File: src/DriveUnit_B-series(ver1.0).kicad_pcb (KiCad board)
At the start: 2 copper layers, 65.7 x 51 mm, 57 parts, among them IC1 A3921, SW1 TVAF06-A020B-R, SW2 TVAF06-A020B-R, SW3 THAF01-NC-R, SW4 SS-12D00G3

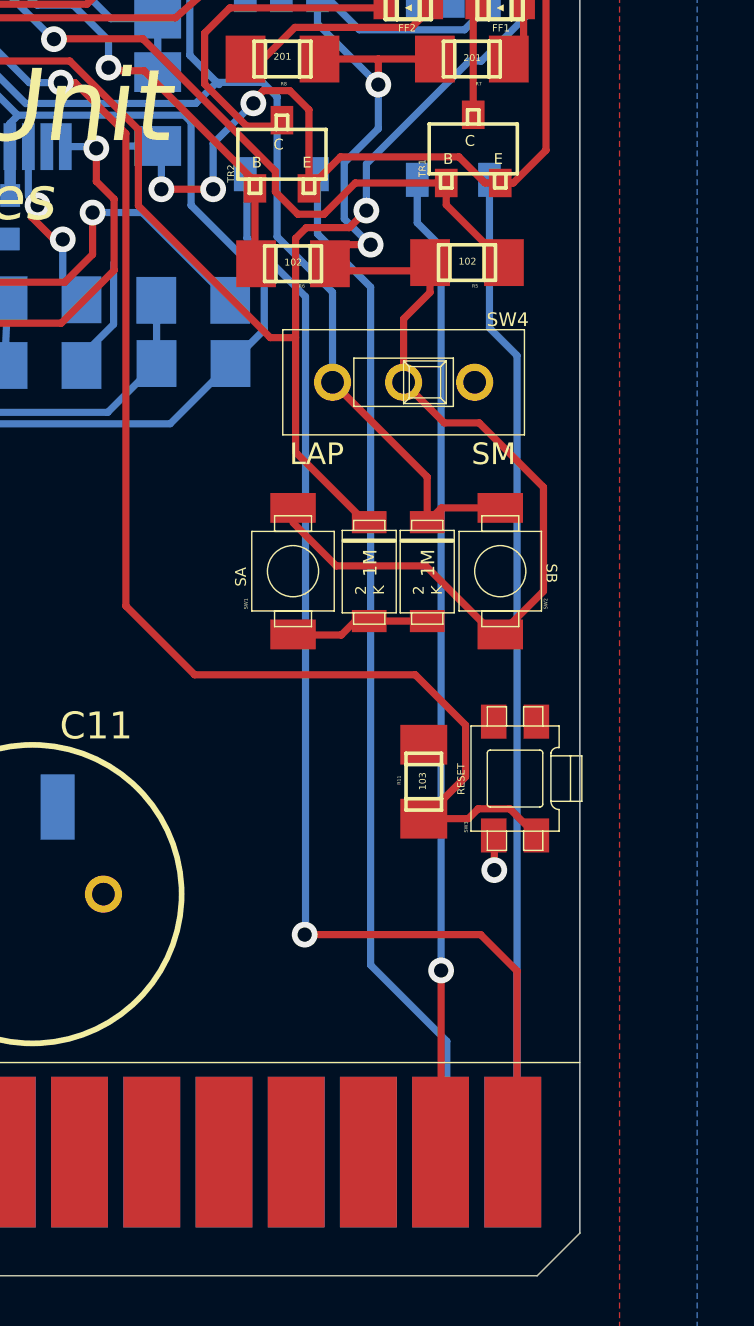
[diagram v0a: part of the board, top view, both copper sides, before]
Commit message: フォトカプラLED入力に200ohm抵抗付けた
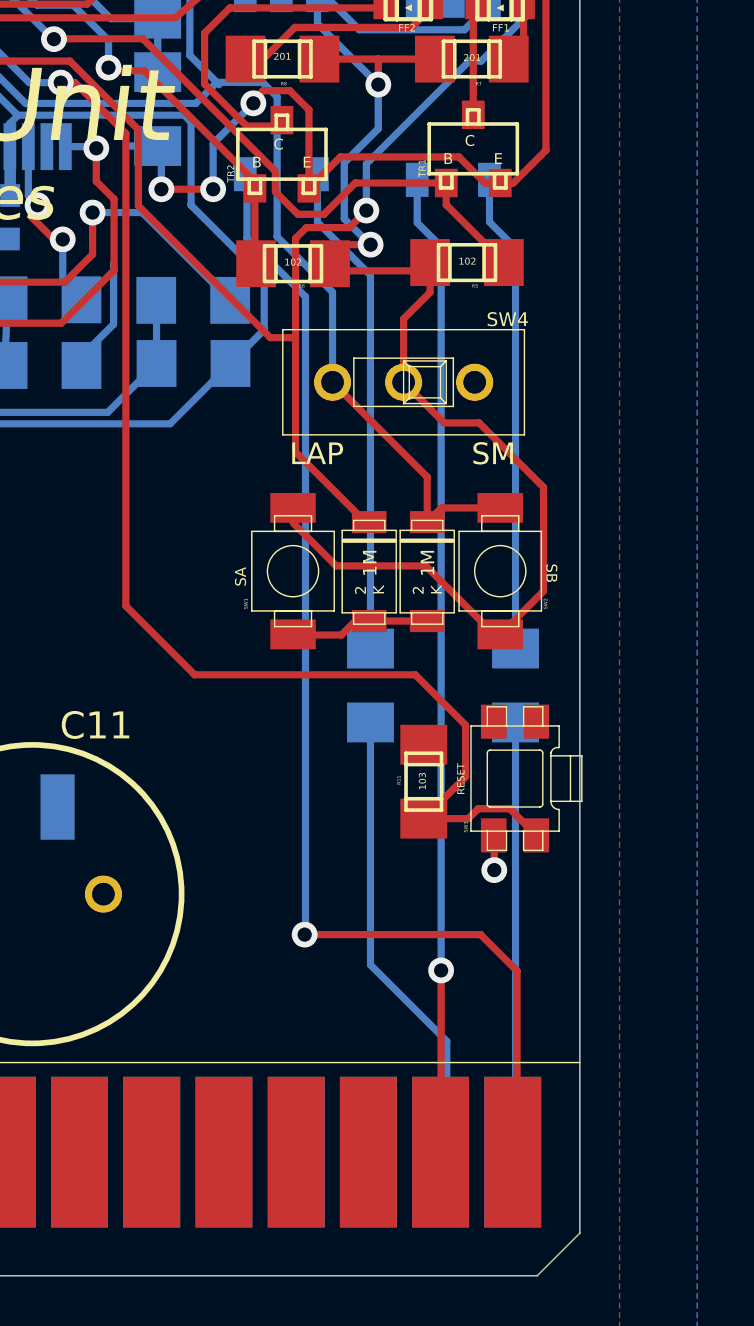
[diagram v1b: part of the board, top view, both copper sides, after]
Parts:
- added R17: RG2012N-201-W-T1, DriveUnit_B-series(ver1.0):RG2012, B.Cu at (174.0, 108.4)
- added R4: RG2012N-201-W-T1, DriveUnit_B-series(ver1.0):RG2012, B.Cu at (179.1, 108.4)
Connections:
- TLP1 pad 1: /DIR_IN -> Net-(R4-PadLEFT)
- TLP2 pad 1: /VCC_IN -> Net-(R17-PadLEFT)
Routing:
- net /VCC_IN: track 36.4 -> 16.3 mm
- net /DIR_IN: track 34.7 -> 15.4 mm
- net Net-(R17-PadLEFT): track 0.00 -> 17.5 mm
- net Net-(R4-PadLEFT): track 0.00 -> 16.9 mm

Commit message: シルクの修正
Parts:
- moved C10 1.36 mm to (153.5, 108.8), turned to 180 degrees
- moved C11 0.74 mm to (162.0, 116.3)
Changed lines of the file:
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@@
     (add_net VCC)
+  )
+  (module "彼女(仮)_回路図:35PZJ330M10X9" (layer Top)
+    (at 161.96 116.35 90)
+    (fp_text reference C11 (at 4.83876 5.74752 180) (layer F.SilkS)
+      (effects (font (size 0.95 0.95) (thickness 0.076)) (justify right bottom))
+    )
+    (fp_text value 35PZJ330M10X9 (at 0 0 90) (layer F.SilkS) hide
+      (effects (font (size 1.27 1.27) (thickness 0.15)))
+    )
+    (fp_circle (center 0 0) (end 5.25 0) (layer F.SilkS) (width 0.2))
+    (fp_line (start 5.2705 0) (end -5.25 0) (layer F.SilkS) (width 0.12))
+    (fp_poly (pts (xy 5.24 0.64) (xy 5.06 1.47) (xy 4.75 2.26) (xy 4.38 2.89)
+      (xy 3.85 3.56) (xy 3.01 4.28) (xy 2.15 4.77) (xy 0.89 5.18)
+      (xy -0.23 5.27) (xy -1.28 5.1) (xy -2.65 4.55) (xy -3.62 3.85)
+      (xy -4.63 2.58) (xy -5.03 1.62) (xy -5.22 0.58) (xy -5.25 0)
+      (xy 5.2705 0)) (layer F.SilkS) (width 0.1))
+    (pad C thru_hole circle (at 0 2.5 90) (size 1.308 1.308) (drill 0.8) (layers *.Cu *.Mask)
+      (net 2 GND) (solder_mask_margin 0.1016))
+    (pad A thru_hole circle (at 0 -2.5 90) (size 1.308 1.308) (drill 0.8) (layers *.Cu *.Mask)
+      (net 1 VCC) (solder_mask_margin 0.1016))
+  )
+  (module "彼女(仮)_回路図:35PZJ330M10X9" (layer Top)
+    (at 153.511218 108.784261 180)
+    (fp_text reference C10 (at 3.051218 4.514261 180) (layer F.SilkS)
+      (effects (font (size 0.95 0.95) (thickness 0.076)) (justify right bottom))
+    )
+    (fp_text value 35PZJ330M10X9 (at 0 0) (layer F.SilkS) hide
+      (effects (font (size 1.27 1.27) (thickness 0.15)))
+    )
+    (fp_circle (center 0 0) (end 5.25 0) (layer F.SilkS) (width 0.2))
+    (fp_line (start -5.25 0) (end 5.25 0) (layer F.SilkS) (width 0.12))
+    (fp_poly (pts (xy 5.26 0.16) (xy 5.11 1.23) (xy 4.77 2.28) (xy 4.06 3.4)
+      (xy 2.63 4.62) (xy 1.36 5.16) (xy -0.5 5.27) (xy -1.93 4.9)
+      (xy -3.31 4.14) (xy -4.08 3.35) (xy -4.64 2.55) (xy -4.98 1.76)
+      (xy -5.17 0.99) (xy -5.25 0) (xy 5.25 0)) (layer F.SilkS) (width 0.1))
+    (pad A thru_hole circle (at 0 -2.5 180) (size 1.308 1.308) (drill 0.8) (layers *.Cu *.Mask)
+      (net 1 VCC) (solder_mask_margin 0.1016))
+    (pad C thru_hole circle (at 0 2.5 180) (size 1.308 1.308) (drill 0.8) (layers *.Cu *.Mask)
+      (net 2 GND) (solder_mask_margin 0.1016))
   )
   (module "DriveUnit_B-series(ver1.0):RG2012" (layer Bottom)
@@
       (net 13 "Net-(C6-PadP$1)") (solder_mask_margin 0.1016))
   )
-  (module "彼女(仮)_回路図:35PZJ330M10X9" (layer Top)
-    (at 152.273 108.21924 140)
-    (fp_text reference C10 (at 1.397351 5.624739 320) (layer F.SilkS)
-      (effects (font (size 0.95 0.95) (thickness 0.076)) (justify left bottom))
-    )
-    (fp_text value 35PZJ330M10X9 (at 0 0 140) (layer F.SilkS) hide
-      (effects (font (size 1.27 1.27) (thickness 0.15)))
-    )
-    (fp_circle (center 0 0) (end 5.25 0) (layer F.SilkS) (width 0.2))
-    (fp_line (start 5 -4) (end 6.5 -4) (layer F.SilkS) (width 0.1524))
-    (fp_line (start 5.75 -4.75) (end 5.75 -3.25) (layer F.SilkS) (width 0.1524))
-    (fp_circle (center 5.75 -4) (end 6.75 -4) (layer F.SilkS) (width 0.1))
-    (pad A thru_hole circle (at 0 -2.5 140) (size 1.308 1.308) (drill 0.8) (layers *.Cu *.Mask)
-      (net 1 VCC) (solder_mask_margin 0.1016))
-    (pad C thru_hole circle (at 0 2.5 140) (size 1.308 1.308) (drill 0.8) (layers *.Cu *.Mask)
-      (net 2 GND) (solder_mask_margin 0.1016))
-  )
-  (module "彼女(仮)_回路図:35PZJ330M10X9" (layer Top)
-    (at 162.08248 117.07876 90)
-    (fp_text reference C11 (at 5.36 0.959996) (layer F.SilkS)
-      (effects (font (size 0.95 0.95) (thickness 0.076)) (justify left bottom))
-    )
-    (fp_text value 35PZJ330M10X9 (at 0 0 90) (layer F.SilkS) hide
-      (effects (font (size 1.27 1.27) (thickness 0.15)))
-    )
-    (fp_circle (center 5.75 -4) (end 6.75 -4) (layer F.SilkS) (width 0.1))
-    (fp_line (start 5.75 -4.75) (end 5.75 -3.25) (layer F.SilkS) (width 0.1524))
-    (fp_line (start 5 -4) (end 6.5 -4) (layer F.SilkS) (width 0.1524))
-    (fp_circle (center 0 0) (end 5.25 0) (layer F.SilkS) (width 0.2))
-    (pad C thru_hole circle (at 0 2.5 90) (size 1.308 1.308) (drill 0.8) (layers *.Cu *.Mask)
-      (net 2 GND) (solder_mask_margin 0.1016))
-    (pad A thru_hole circle (at 0 -2.5 90) (size 1.308 1.308) (drill 0.8) (layers *.Cu *.Mask)
-      (net 1 VCC) (solder_mask_margin 0.1016))
-  )
   (module "彼女(仮)_回路図:GRM21BC72A105KE01" (layer Bottom)
